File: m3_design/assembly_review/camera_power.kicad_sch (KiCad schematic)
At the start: 22 parts, among them U7 TPS259570DSGR, U8 AP63300WU-7

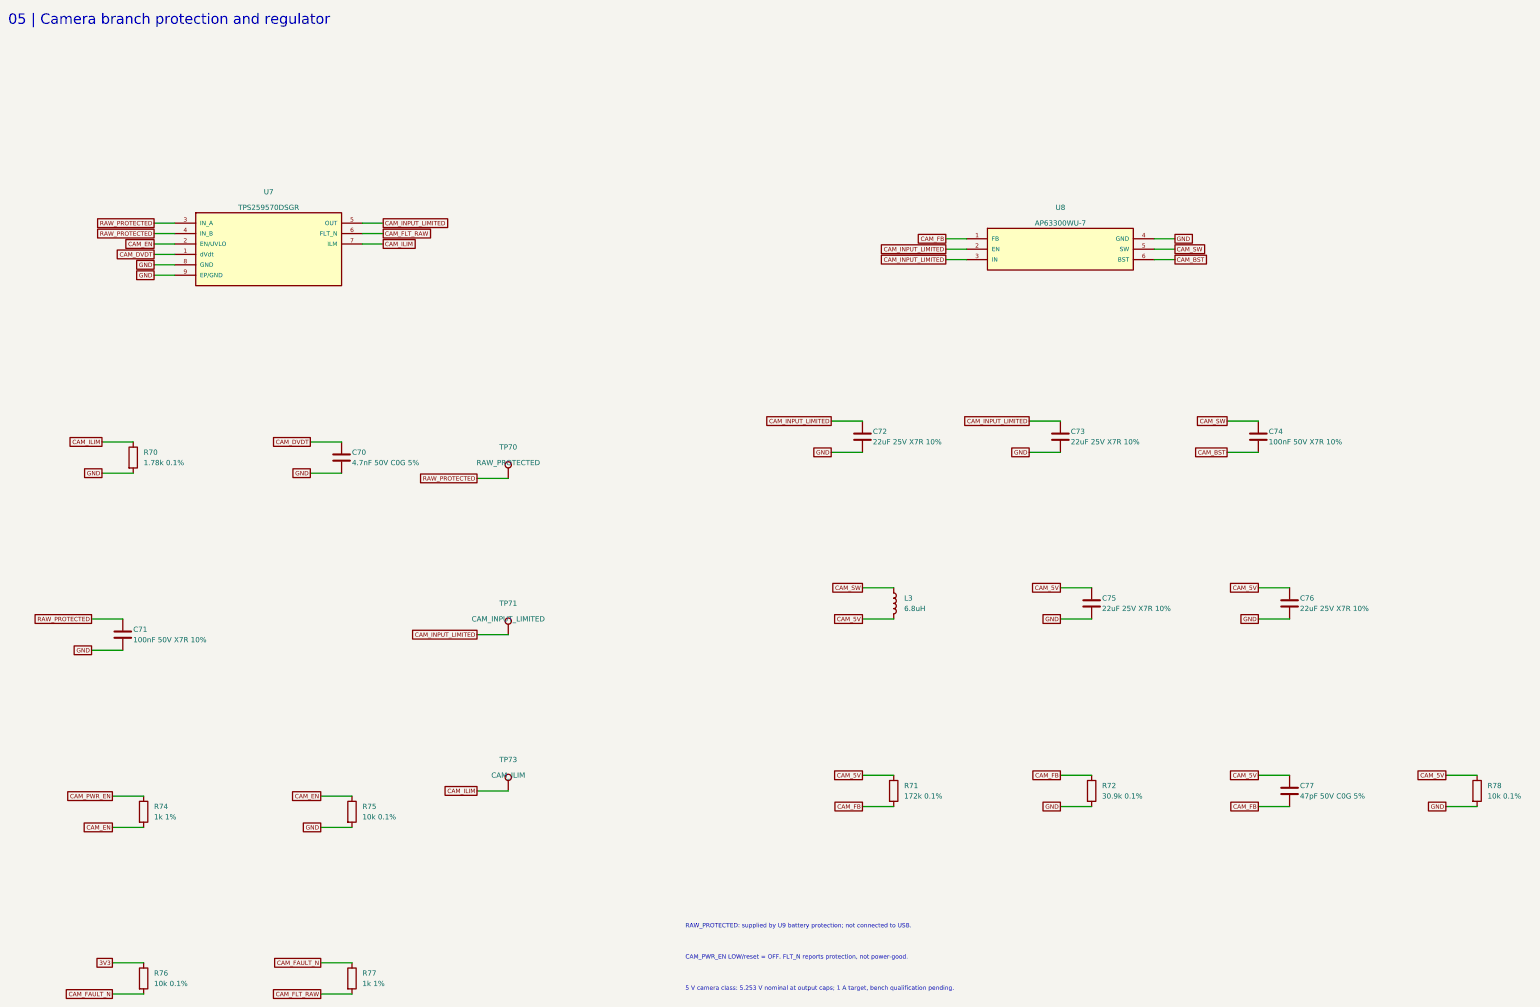
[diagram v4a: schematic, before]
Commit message: M3-ASSY-R4: R3 validation fixes, new IMU, fault-tolerant pyro sensing
The board, schematic sheets and footprint library are generated from
R3 (533af8e) by m3_design/r4_build.sh (r4_lib.py, r4_sch.py,
r4_pcb.py). docs/REQUIREMENTS.md states what the board must do;
docs/M3_R4.md records every change, the thirteen evaluation passes
(twelve independent reviews) and the accepted deviations.

- IMU: ST LSM6DSV320X (16 g and 320 g, 4000 dps)
- Pyro: black ARM and orange igniter terminals, eight pyro spacing
  rules in m3.kicad_dru, sense dividers of 2 x 5.1k over 2 x 2k in
  parallel, 4.7k at each ADC pin (R168-R172)
- Pull-pin on a JST PH connector; JLC tooling holes
- Fab: Standard PCBA, 84 BOM lines, 205 placed parts, $80.12 per board
  at five boards (tools/jlc_cost.py); placement rotations verified
- Gate: tools/check.sh DRC 0, unconnected 0, schematic parity 0, ERC 0,
  audit OK; m3_design/check_actuators.py OK

Nothing has been built or measured, and there is no R4 firmware. The
open owner decisions and the bench tests are listed in STATUS.md.

Co-Authored-By: Claude Opus 5.5 <noreply@anthropic.com>
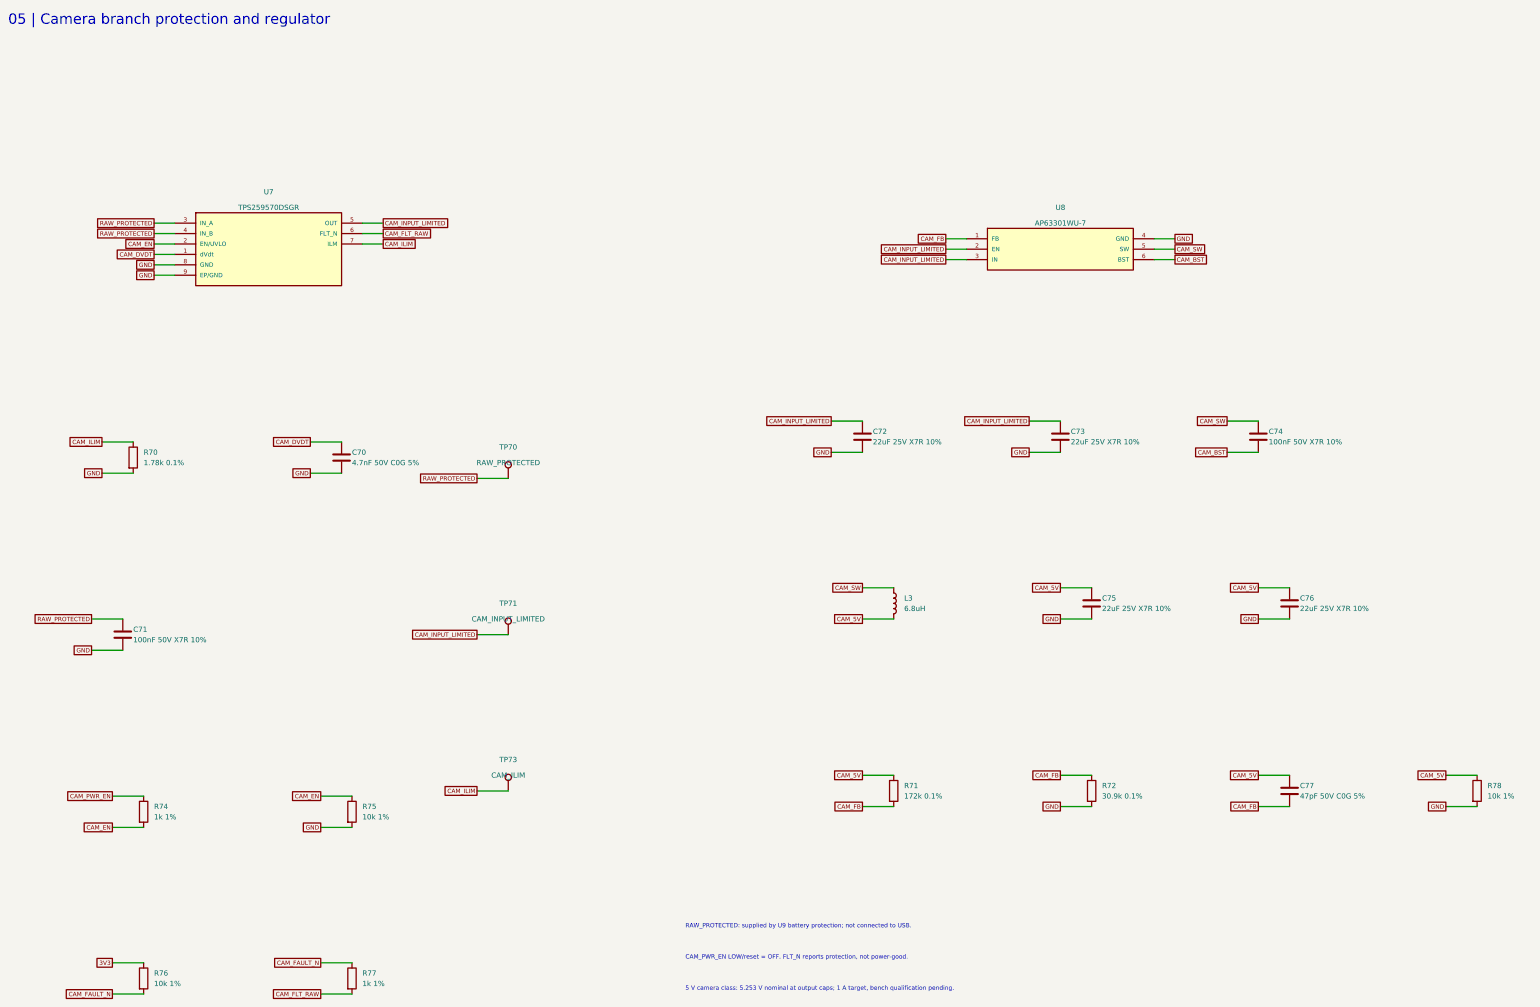
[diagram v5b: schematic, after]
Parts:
- C71, C74: LCSC C1591 -> C14663; LCSC Part C1591 -> C14663; Manufacturer Samsung Electro-Mechanics -> YAGEO; Manufacturer Part CL10B104KB8NNNC -> CC0603KRX7R9BB104
- R75, R76, R78: value 10k 0.1% -> 10k 1%; LCSC C95204 -> C25804; LCSC Part C95204 -> C25804; Manufacturer Yageo -> UNI-ROYAL(Uniroyal Elec); Manufacturer Part RT0603BRD0710KL -> 0603WAF1002T5E
- U8: value AP63300WU-7 -> AP63301WU-7; LCSC C2158012 -> C2158003; Manufacturer (none) -> Diodes Incorporated; Manufacturer Part (none) -> AP63301WU-7
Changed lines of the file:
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@@
 		(title "05 | Camera branch protection and regulator")
 		(date "2026-09-07")
-		(rev "M3-ASSY-R3")
+		(rev "M3-ASSY-R4")
 		(company "Single-board M3 candidate; full system incomplete"))
 	(text "05 | Camera branch protection and regulator"
@@
 				(font
 					(size 1.27 1.27))))
-		(property "Value" "AP63300WU-7"
+		(property "Value" "AP63301WU-7"
 			(at 276.86 69.85 0)
 			(effects
@@
 				(font
 					(size 1.27 1.27))))
-		(property "LCSC" "C2158012"
+		(property "LCSC" "C2158003"
 			(at 276.86 76.2 0)
 			(hide yes)
@@
 				(font
 					(size 1.27 1.27))))
+		(property "Manufacturer" "Diodes Incorporated"
+			(at 276.86 76.2 0)
+			(hide yes)
+			(effects
+				(font
+					(size 1.27 1.27))
+				(justify left)))
+		(property "Manufacturer Part" "AP63301WU-7"
+			(at 276.86 76.2 0)
+			(hide yes)
+			(effects
+				(font
+					(size 1.27 1.27))
+				(justify left)))
 		(instances
 			(project "m3"
@@
 					(size 1.27 1.27))
 				(justify left)))
-		(property "LCSC" "C1591"
+		(property "LCSC" "C14663"
 			(at 48.26 170.18 0)
 			(hide yes)
@@
 					(reference "C71")
 					(unit 1))))
-		(property "Manufacturer" "Samsung Electro-Mechanics"
+		(property "Manufacturer" "YAGEO"
 			(at 48.26 170.18 0)
 			(hide yes)
@@
 				(font
 					(size 1.27 1.27))))
-		(property "Manufacturer Part" "CL10B104KB8NNNC"
+		(property "Manufacturer Part" "CC0603KRX7R9BB104"
 			(at 48.26 170.18 0)
 			(hide yes)
@@
 				(font
 					(size 1.27 1.27))))
-		(property "LCSC Part" "C1591"
+		(property "LCSC Part" "C14663"
 			(at 48.26 170.18 0)
 			(hide yes)
@@
 					(size 1.27 1.27))
 				(justify left)))
-		(property "LCSC" "C1591"
+		(property "LCSC" "C14663"
 			(at 325.12 121.92 0)
 			(hide yes)
@@
 					(reference "C74")
 					(unit 1))))
-		(property "Manufacturer" "Samsung Electro-Mechanics"
+		(property "Manufacturer" "YAGEO"
 			(at 325.12 121.92 0)
 			(hide yes)
@@
 				(font
 					(size 1.27 1.27))))
-		(property "Manufacturer Part" "CL10B104KB8NNNC"
+		(property "Manufacturer Part" "CC0603KRX7R9BB104"
 			(at 325.12 121.92 0)
 			(hide yes)
@@
 				(font
 					(size 1.27 1.27))))
-		(property "LCSC Part" "C1591"
+		(property "LCSC Part" "C14663"
 			(at 325.12 121.92 0)
 			(hide yes)
@@
 					(size 1.27 1.27))
 				(justify left)))
-		(property "Value" "10k 0.1%"
+		(property "Value" "10k 1%"
 			(at 106.68 214.63 0)
 			(effects
@@
 					(size 1.27 1.27))
 				(justify left)))
-		(property "LCSC" "C95204"
+		(property "LCSC" "C25804"
 			(at 104.14 213.36 0)
 			(hide yes)
@@
 					(reference "R75")
 					(unit 1))))
-		(property "Manufacturer" "Yageo"
+		(property "Manufacturer" "UNI-ROYAL(Uniroyal Elec)"
 			(at 104.14 213.36 0)
 			(hide yes)
@@
 				(font
 					(size 1.27 1.27))))
-		(property "Manufacturer Part" "RT0603BRD0710KL"
+		(property "Manufacturer Part" "0603WAF1002T5E"
 			(at 104.14 213.36 0)
 			(hide yes)
@@
 				(font
 					(size 1.27 1.27))))
-		(property "LCSC Part" "C95204"
+		(property "LCSC Part" "C25804"
 			(at 104.14 213.36 0)
 			(hide yes)
@@
 					(size 1.27 1.27))
 				(justify left)))
-		(property "Value" "10k 0.1%"
+		(property "Value" "10k 1%"
 			(at 55.88 255.26999999999998 0)
 			(effects
@@
 					(size 1.27 1.27))
 				(justify left)))
-		(property "LCSC" "C95204"
+		(property "LCSC" "C25804"
 			(at 53.34 254 0)
 			(hide yes)
@@
 					(reference "R76")
 					(unit 1))))
-		(property "Manufacturer" "Yageo"
+		(property "Manufacturer" "UNI-ROYAL(Uniroyal Elec)"
 			(at 53.34 254 0)
 			(hide yes)
@@
 				(font
 					(size 1.27 1.27))))
-		(property "Manufacturer Part" "RT0603BRD0710KL"
+		(property "Manufacturer Part" "0603WAF1002T5E"
 			(at 53.34 254 0)
 			(hide yes)
@@
 				(font
 					(size 1.27 1.27))))
-		(property "LCSC Part" "C95204"
+		(property "LCSC Part" "C25804"
 			(at 53.34 254 0)
 			(hide yes)
@@
 					(size 1.27 1.27))
 				(justify left)))
-		(property "Value" "10k 0.1%"
+		(property "Value" "10k 1%"
 			(at 381.0 209.54999999999998 0)
 			(effects
@@
 					(size 1.27 1.27))
 				(justify left)))
-		(property "LCSC" "C95204"
+		(property "LCSC" "C25804"
 			(at 378.46 208.28 0)
 			(hide yes)
@@
 					(reference "R78")
 					(unit 1))))
-		(property "Manufacturer" "Yageo"
+		(property "Manufacturer" "UNI-ROYAL(Uniroyal Elec)"
 			(at 378.46 208.28 0)
 			(hide yes)
@@
 				(font
 					(size 1.27 1.27))))
-		(property "Manufacturer Part" "RT0603BRD0710KL"
+		(property "Manufacturer Part" "0603WAF1002T5E"
 			(at 378.46 208.28 0)
 			(hide yes)
@@
 				(font
 					(size 1.27 1.27))))
-		(property "LCSC Part" "C95204"
+		(property "LCSC Part" "C25804"
 			(at 378.46 208.28 0)
 			(hide yes)
